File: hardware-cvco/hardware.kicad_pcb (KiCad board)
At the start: 4 copper layers, 100 x 70 mm, 163 parts, among them J1 SMA, J2 SMA, J3 SMA, J4 SMA, J5 SMA, J6 SMA, J7 SMA, J8 Pickit 2, J9 DC, Q1 AOD403, Q2 PN2222A, SW1 On/Off, U13 PIC12F675-ISN, U14 NLB-310-T1, U15 NLB-310-T1, U16 NLB-310-T1, U17 LM358, U18 LM317DCYR, U19 MCP73871-2AA, U2 74LS07, U20 TPS61046, U21 LM386, U6 NLB-310-T1, U7 NLB-310-T1, U8 NLB-310-T1, U9 NLB-310-T1, Y1 CVCO55CW-0100-0200, Y2 CVCO55CW-0200-0500, Y3 CV55CW500-1000, Y4 CVCO55CW-1000-2000, Y5 CV55BE1600-3200, Y6 CVCO55CC-3180-3710, Y7 CVCO55CW-3500-4500

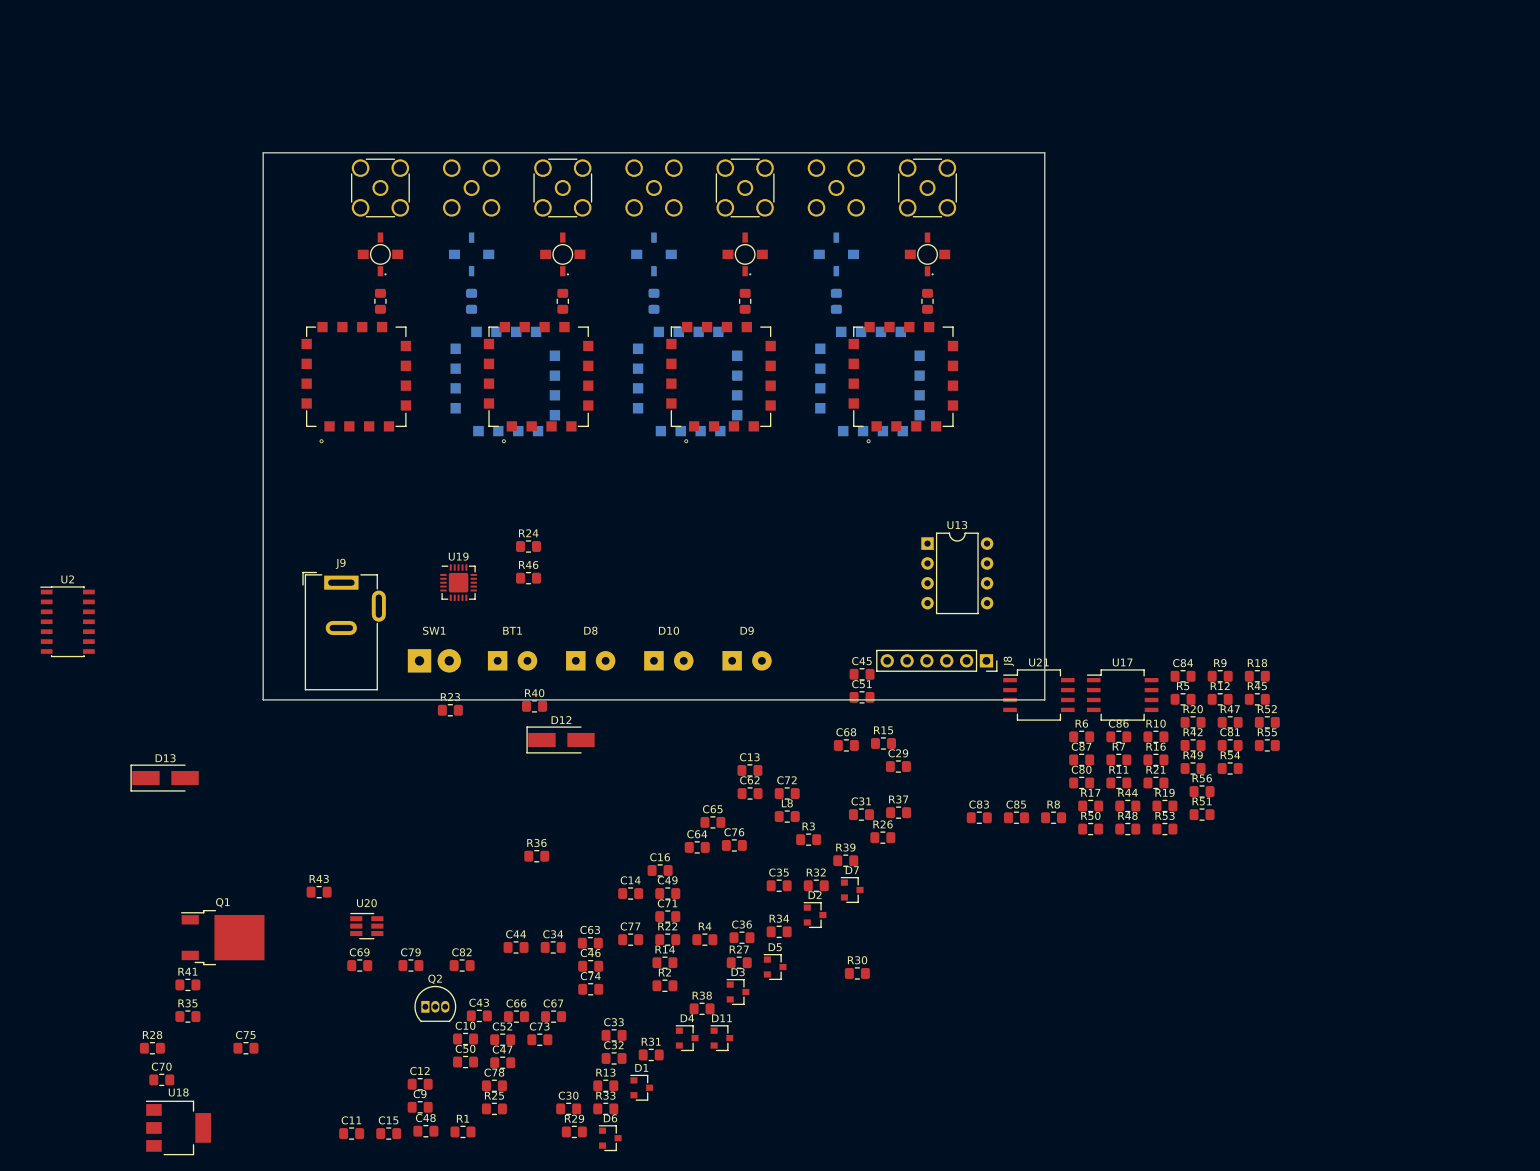
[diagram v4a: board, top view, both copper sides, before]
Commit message: RF section layout finished - CVCO.
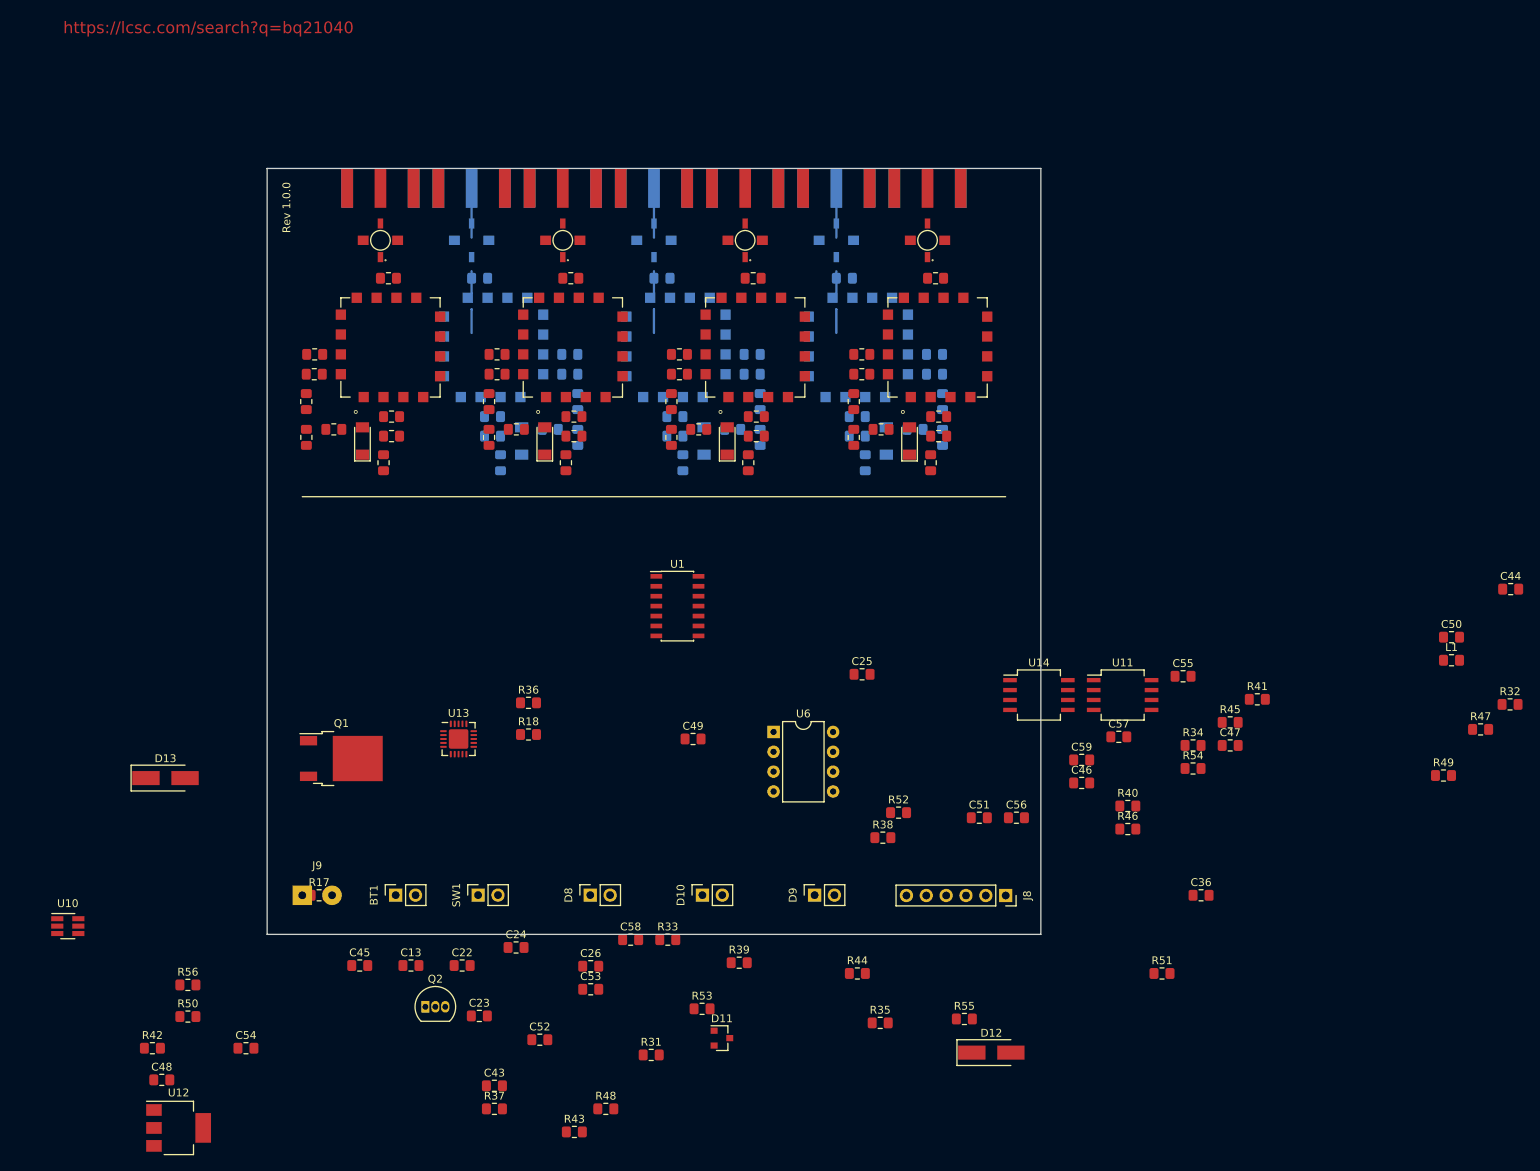
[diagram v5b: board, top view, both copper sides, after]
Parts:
- removed the R19 at (180.4, 133.6)
- removed the R7 at (174.5, 127.7)
- removed the U2 at (40.0, 110.0)
- added R15: 680, Resistor_SMD:R_0805_2012Metric_Pad1.15x1.40mm_HandSolder, F.Cu at (117.2, 81.8)
- added R9: 1k, Resistor_SMD:R_0805_2012Metric_Pad1.15x1.40mm_HandSolder, F.Cu at (74.0, 85.4)
- added U1: 74LS07, Package_SO:SOIC-14_3.9x8.7mm_P1.27mm, F.Cu at (118.0, 108.0)
- BT1, D10, D8, D9: footprint Connector_Wire:SolderWirePad_1x02_P3.81mm_Drill1mm -> Connector_PinSocket_2.54mm:PinSocket_1x02_P2.54mm_Vertical
- C27: renamed from C47; moved to B.Cu
- C28: renamed from C48; moved to B.Cu
- C29: renamed from C49; moved to B.Cu
- C30: renamed from C50; moved to B.Cu
- C31: renamed from C51; moved to B.Cu
- C32: renamed from C52; moved to B.Cu
- C37: renamed from C62; moved to B.Cu
- C38: renamed from C63; moved to B.Cu
- C39: renamed from C64; moved to B.Cu
- C40: renamed from C65; moved to B.Cu
- C41: renamed from C66; moved to B.Cu
- C42: renamed from C67; moved to B.Cu
- D1, D2, D3, D4: footprint Package_TO_SOT_SMD:SOT-23 -> Diode_SMD:D_MiniMELF
- D5, D6, D7: footprint Package_TO_SOT_SMD:SOT-23 -> Diode_SMD:D_MiniMELF; moved to B.Cu
- J1, J2, J3, J4, J5, J6, J7: footprint Connector_Coaxial:SMA_Amphenol_132134_Vertical -> CVCO:SMA-Edge
- J9: footprint Connector_BarrelJack:BarrelJack_Wuerth_6941xx301002 -> Connector_Wire:SolderWirePad_1x02_P3.81mm_Drill1mm
- R19: renamed from R13; moved to B.Cu
- R20: renamed from R14; moved to B.Cu
- R21: renamed from R15; moved to B.Cu
- R22: renamed from R51; moved to B.Cu
- R23: renamed from R52; moved to B.Cu
- R24: renamed from R53; moved to B.Cu
- R25: renamed from R54; moved to B.Cu
- R26: renamed from R55; moved to B.Cu
- R27: renamed from R56; moved to B.Cu
- R28: renamed from R16; moved to B.Cu
- R29: renamed from R17; moved to B.Cu
- R30: renamed from R18; moved to B.Cu
- SW1: footprint Connector_Wire:SolderWirePad_1x02_P3.81mm_Drill1.2mm -> Connector_PinSocket_2.54mm:PinSocket_1x02_P2.54mm_Vertical
- moved R5 120.8 mm to (70.5, 86.4), turned to 270 degrees
- moved R13 118.5 mm to (70.5, 81.8), turned to 270 degrees
- moved C7 114.5 mm to (141.6, 78.3)
- moved C32 103.6 mm to (150.9, 75.8), turned to 180 degrees
- moved C28 101.1 mm to (104.2, 75.8), turned to 180 degrees
- moved C3 98.9 mm to (94.9, 78.3)
- moved R25 97.2 mm to (101.7, 85.4), turned to 180 degrees
- moved C30 95.3 mm to (127.6, 78.3), turned to 180 degrees
- moved C1 94.8 mm to (71.5, 78.3)
- moved R10 94.4 mm to (97.4, 85.4)
- moved C4 93.9 mm to (94.9, 75.8)
- moved R6 93.5 mm to (93.9, 86.4), turned to 270 degrees
- moved R22 93.3 mm to (105.3, 86.4), turned to 270 degrees
- moved C15 91.4 mm to (81.4, 83.8)
- moved D1 90.1 mm to (77.7, 86.9), turned to 90 degrees
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- renumbered C9 to C1, C26 to C10, C27 to C11, C28 to C12, C79 to C13, C29 to C14, C30 to C15, C31 to C16, C32 to C17, C33 to C18, C34 to C19, C10 to C2, C35 to C20, C36 to C21, C82 to C22, C43 to C23, C44 to C24, C45 to C25, C46 to C26, C11 to C3, C59 to C33, C60 to C34, C61 to C35, C76 to C36, C12 to C4, C78 to C43, C68 to C44, C69 to C45, C80 to C46, C81 to C47, C70 to C48, C71 to C49, C13 to C5, C72 to C50, C83 to C51, C73 to C52, C74 to C53, C75 to C54, C84 to C55, C85 to C56, C86 to C57, C77 to C58, C87 to C59, C14 to C6, C15 to C7, C16 to C8, C25 to C9, L8 to L1, R20 to R10, R21 to R11, R50 to R12, R5 to R13, R6 to R14, R8 to R16, R43 to R17, R46 to R18, R39 to R32, R22 to R33, R42 to R34, R23 to R35, R24 to R36, R25 to R37, R26 to R38, R27 to R39, R44 to R40, R45 to R41, R28 to R42, R29 to R43, R30 to R44, R47 to R45, R48 to R46, R32 to R47, R33 to R48, R34 to R49, R9 to R5, R35 to R50, R36 to R51, R37 to R52, R38 to R53, R49 to R54, R40 to R55, R41 to R56, R10 to R6, R11 to R7, R12 to R8, U20 to U10, U17 to U11, U18 to U12, U19 to U13, U21 to U14, U6 to U2, U7 to U3, U8 to U4, U9 to U5, U13 to U6, U14 to U7, U15 to U8, U16 to U9
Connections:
- C1 pad 1: Net-(C10-Pad1) (its old number) -> Net-(C1-Pad1)
- C2 pad 1: Net-(C10-Pad1) (its old number) -> Net-(C1-Pad1)
- C27 pad 1: Net-(C47-Pad1) -> Net-(C27-Pad1)
- C28 pad 1: Net-(C47-Pad1) -> Net-(C27-Pad1)
- C29 pad 1: Net-(C49-Pad1) -> Net-(C29-Pad1)
- C3 pad 1: Net-(C11-Pad1) (its old number) -> Net-(C3-Pad1)
- C30 pad 1: Net-(C49-Pad1) -> Net-(C29-Pad1)
- C31 pad 1: Net-(C51-Pad1) (its old number) -> Net-(C31-Pad1)
- C32 pad 1: Net-(C51-Pad1) (its old number) -> Net-(C31-Pad1)
- C4 pad 1: Net-(C11-Pad1) (its old number) -> Net-(C3-Pad1)
- C5 pad 1: Net-(C13-Pad1) (its old number) -> Net-(C5-Pad1)
- C6 pad 1: Net-(C13-Pad1) (its old number) -> Net-(C5-Pad1)
- C7 pad 1: Net-(C15-Pad1) -> Net-(C7-Pad1)
- C8 pad 1: Net-(C15-Pad1) -> Net-(C7-Pad1)
- J1 pad 1: P2_VSS -> Net-(C1-Pad1)
- J2 pad 1: P2_VSS -> Net-(C3-Pad1)
- J3 pad 1: P2_VSS -> Net-(C5-Pad1)
- J4 pad 1: P2_VSS -> Net-(C7-Pad1)
- J5 pad 1: P2_VSS -> Net-(C27-Pad1)
- J6 pad 1: P2_VSS -> Net-(C29-Pad1)
- J7 pad 1: P2_VSS -> Net-(C31-Pad1)
- R13 pad 1: Net-(C10-Pad1) (its old number) -> Net-(C1-Pad1)
- R14 pad 1: Net-(C11-Pad1) (its old number) -> Net-(C3-Pad1)
- R16 pad 1: Net-(C15-Pad1) -> Net-(C7-Pad1)
- R28 pad 1: Net-(C47-Pad1) -> Net-(C27-Pad1)
- R29 pad 1: Net-(C49-Pad1) -> Net-(C29-Pad1)
- R30 pad 1: Net-(C51-Pad1) (its old number) -> Net-(C31-Pad1)
- U2 pad 3: P2_VSS -> Net-(C1-Pad1)
- U3 pad 3: P2_VSS -> Net-(C3-Pad1)
- U4 pad 3: P2_VSS -> Net-(C5-Pad1)
- U5 pad 3: P2_VSS -> Net-(C7-Pad1)
- U7 pad 3: P2_VSS -> Net-(C27-Pad1)
- U8 pad 3: P2_VSS -> Net-(C29-Pad1)
- U9 pad 3: P2_VSS -> Net-(C31-Pad1)
- Y1 pad 14: P2_VSS -> Net-(C1-Pad1)
- Y2 pad 14: P2_VSS -> Net-(C3-Pad1)
- Y3 pad 14: P2_VSS -> Net-(C5-Pad1)
- Y4 pad 14: P2_VSS -> Net-(C7-Pad1)
- Y5 pad 14: P2_VSS -> Net-(C27-Pad1)
- Y6 pad 14: P2_VSS -> Net-(C29-Pad1)
- Y7 pad 14: P2_VSS -> Net-(C31-Pad1)
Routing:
- net P2_VSS: track 0.00 -> 9.08 mm
- net Net-(C31-Pad1): track 0.00 -> 6.35 mm
- net Net-(C29-Pad1): track 0.00 -> 6.35 mm
- net Net-(C27-Pad1): track 0.00 -> 6.35 mm
- net Net-(C35-Pad1): track 0.00 -> 2.82 mm
- net Net-(C34-Pad1): track 0.00 -> 2.82 mm
- net Net-(C33-Pad1): track 0.00 -> 2.82 mm
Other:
- board size 100 x 70 mm -> 99 x 98 mm
- board text added: "Rev 1.0.0"
- board text added: "https://lcsc.com/search?q=bq21040"

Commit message: Added horizontal Molex footprint & 3D model.
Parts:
- BT1, D10, D8, D9, SW1: footprint Connector_PinSocket_2.54mm:PinSocket_1x02_P2.54mm_Vertical -> CVCO:2-2.54mm-Horizontal-Molex
- D1: value 5V -> 5.1V
- Q2: value PN2222A -> MBT2222; footprint Package_TO_SOT_THT:TO-92_Inline -> Package_TO_SOT_SMD:SOT-23
- moved C36 186.1 mm to (0.00, 125.0)
- moved C44 186.1 mm to (39.6, 85.8)
- moved C46 186.1 mm to (-15.3, 110.6)
- moved C47 186.1 mm to (3.73, 105.8)
- moved C50 186.1 mm to (32.0, 92.0)
- moved C55 186.1 mm to (-2.30, 97.0)
- moved C57 186.1 mm to (-10.5, 104.7)
- moved C59 186.1 mm to (-15.3, 107.7)
- moved L1 186.1 mm to (32.0, 94.9)
- moved R32 186.1 mm to (39.5, 100.6)
- moved R34 186.1 mm to (-1.02, 105.8)
- moved R40 186.1 mm to (-9.37, 113.6)
- moved R41 186.1 mm to (7.20, 99.9)
- moved R45 186.1 mm to (3.73, 102.9)
- moved R46 186.1 mm to (-9.37, 116.5)
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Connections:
- Q1 pad 2: Net-(J9-Pad2) -> Net-(J9-Pad1)
- SW1 pad 1: P2_VSS -> Net-(J9-Pad2)
- SW1 pad 2: Net-(J9-Pad1) -> P2_VSS
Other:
- board text added: "+"
- board text added: "-"
- board text added: "PCB was designed to fit in the following enclosure:"
- board text added: "https://www.hammfg.com/files/parts/pdf/1455L1202BK.pdf"

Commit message: Rough layout of the non-RF section.
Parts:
- added F1: 3A Fast, Fuse:Fuse_1206_3216Metric_Pad1.42x1.75mm_HandSolder, F.Cu at (96.0, 112.0)
- C13, C22, C45, C46, C47, C48, C51, C54, C55, C56, C57, C59, Q2, R17, R34, R35, R36, R40, R41, R42, R44, R45, R46, R50, R51, R54, R55, R56, U11, U14: moved to B.Cu
- D11: value 3V -> 10V; footprint Package_TO_SOT_SMD:SOT-23 -> Diode_SMD:D_MiniMELF
- D13: footprint Diode_SMD:D_SMA_Handsoldering -> Diode_SMD:D_MiniMELF; moved to B.Cu
- U6: footprint Package_DIP:DIP-8_W7.62mm -> Package_SO:SOIC-8_3.9x4.9mm_P1.27mm
- moved C56 181.3 mm to (80.0, 109.0), turned to 270 degrees
- moved C51 156.3 mm to (100.0, 113.0), turned to 270 degrees
- moved R52 133.4 mm to (113.0, 114.0)
- moved C48 124.9 mm to (145.0, 110.0), turned to 270 degrees
- moved R18 123.9 mm to (136.9, 102.4)
- moved U13 123.9 mm to (128.0, 103.0)
- moved R36 121.9 mm to (141.0, 110.0), turned to 270 degrees
- moved R42 117.7 mm to (133.0, 103.0), turned to 270 degrees
- moved R38 113.3 mm to (136.0, 107.0)
- moved R46 112.7 mm to (103.0, 108.0), turned to 270 degrees
- moved R50 111.3 mm to (141.0, 116.0), turned to 270 degrees
- moved C54 110.4 mm to (145.0, 116.0), turned to 270 degrees
- moved C36 109.2 mm to (107.0, 103.0)
- moved C23 106.8 mm to (160.0, 98.0)
- moved C57 105.6 mm to (95.0, 100.0), turned to 270 degrees
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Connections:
- J9 pad 1: Net-(J9-Pad1) -> Net-(F1-Pad1)
- Q1 pad 2: Net-(J9-Pad1) -> Net-(F1-Pad2)
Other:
- board size 99 x 98 mm -> 99 x 75 mm

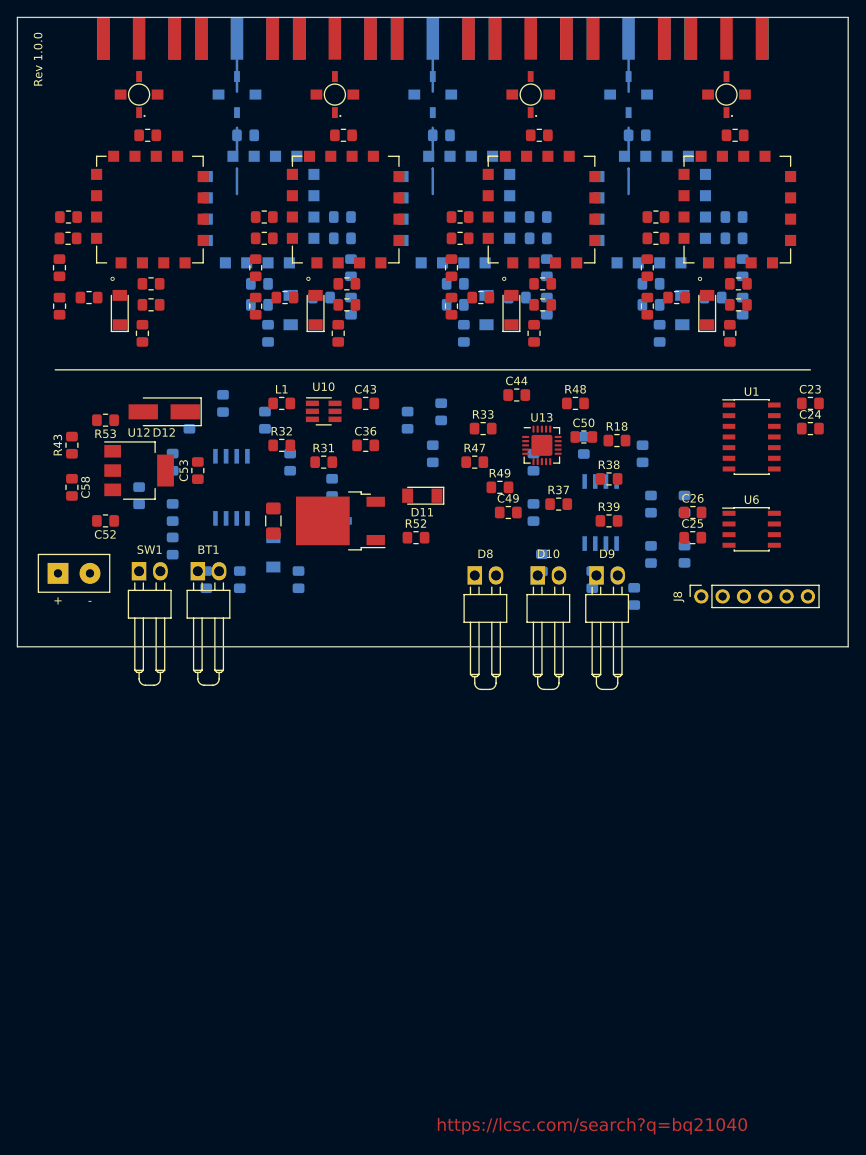
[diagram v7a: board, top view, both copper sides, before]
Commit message: Added icons & icon footprints - CVCO.
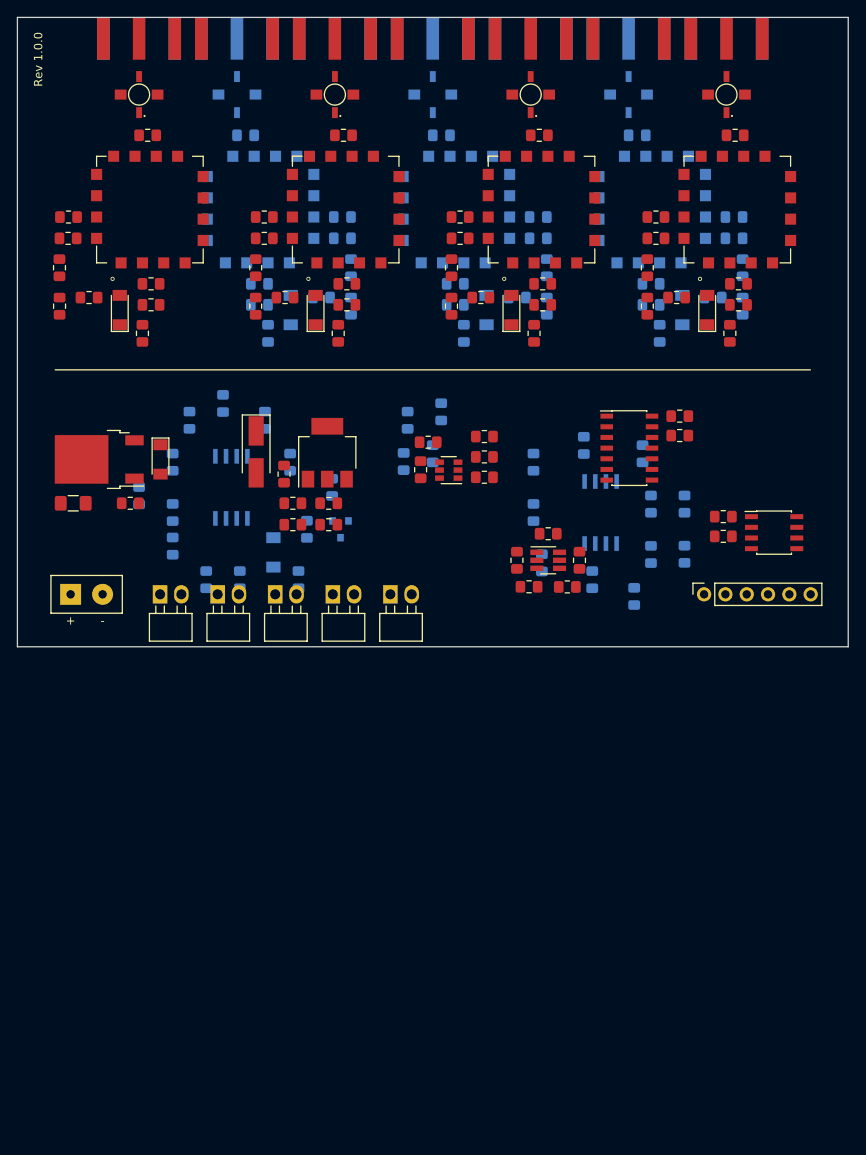
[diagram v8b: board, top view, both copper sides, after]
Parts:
- removed the C44 at (125.0, 97.0)
- removed the C49 at (124.0, 111.0)
- removed the C50 at (133.0, 102.0)
- removed the D10 at (127.5, 118.5)
- removed the R37 at (130.0, 110.0)
- removed the R38 at (136.0, 107.0)
- removed the R39 at (136.0, 112.0)
- removed the R47 at (120.0, 105.0)
- removed the R48 at (132.0, 98.0)
- removed the R49 at (123.0, 108.0)
- removed the U13 at (128.0, 103.0)
- added C45: 1μF, Capacitor_SMD:C_0805_2012Metric_Pad1.15x1.40mm_HandSolder, F.Cu at (121.2, 104.4)
- added C46: 1μF, Capacitor_SMD:C_0805_2012Metric_Pad1.15x1.40mm_HandSolder, F.Cu at (113.5, 105.9)
- added R34: 120, Resistor_SMD:R_0805_2012Metric_Pad1.15x1.40mm_HandSolder, F.Cu at (114.5, 102.6)
- added R36: 120, Resistor_SMD:R_0805_2012Metric_Pad1.15x1.40mm_HandSolder, F.Cu at (121.2, 106.8)
- added TH1: 10k, CVCO:2-2.54mm-Horizontal-Molex, F.Cu at (96.2, 120.8)
- added U11: BQ21040, Package_TO_SOT_SMD:SOT-23-6, F.Cu at (116.9, 106.0)
- D9: value Red -> Orange
- R18: moved to B.Cu
- R33: value 10k -> 15k
- moved R32 38.0 mm to (131.0, 119.9), turned to 180 degrees
- moved L1 35.3 mm to (128.8, 113.5)
- moved R48 34.3 mm to (79.0, 109.9), turned to 180 degrees
- moved U10 32.1 mm to (128.8, 116.7)
- moved C43 31.6 mm to (132.5, 116.7), turned to 270 degrees
- moved D10 31.5 mm to (82.5, 104.7), turned to 270 degrees
- moved Q1 29.7 mm to (75.2, 104.7)
- moved R31 28.6 mm to (126.5, 119.8)
- moved C57 26.7 mm to (98.3, 112.5), turned to 0 degrees
- moved C51 26.7 mm to (102.6, 109.9)
- moved R18 25.5 mm to (111.5, 104.9), turned to 270 degrees
- moved R42 25.5 mm to (97.3, 106.4), turned to 270 degrees
- moved D9 24.7 mm to (109.9, 120.8)
- moved R49 24.4 mm to (98.3, 109.9), turned to 0 degrees
- moved F1 23.9 mm to (72.2, 109.9), turned to 0 degrees
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- renumbered C45 to C44, C46 to C47, C47 to C48, C48 to C49, C51 to C50, C52 to C51, C53 to C52, C54 to C53, C55 to C54, C56 to C55, C57 to C56, C58 to C57, C59 to C58, D11 to D10, D12 to D11, D13 to D12, R34 to R35, R35 to R37, R36 to R38, R40 to R39, R41 to R40, R42 to R41, R43 to R42, R44 to R43, R45 to R44, R46 to R45, R50 to R46, R51 to R47, R52 to R48, R53 to R49, R54 to R50, R55 to R51, R56 to R52, U11 to U12, U12 to U13
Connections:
- BT1 pad 1: Net-(BT1-Pad1) -> BAT
- D9 pad 2: DC -> Net-(D9-Pad2)
- R33 pad 1: DC -> Net-(D9-Pad2)
- R33 pad 2: Net-(R33-Pad2) -> BAT
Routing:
- net P2_VSS: track 9.08 -> 0.00 mm
- net Net-(C31-Pad1): track 6.35 -> 0.00 mm
- net Net-(C29-Pad1): track 6.35 -> 0.00 mm
- net Net-(C27-Pad1): track 6.35 -> 0.00 mm
- net Net-(C35-Pad1): track 2.82 -> 0.00 mm
- net Net-(C34-Pad1): track 2.82 -> 0.00 mm
- net Net-(C33-Pad1): track 2.82 -> 0.00 mm
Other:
- board text removed: "https://lcsc.com/search?q=bq21040"
